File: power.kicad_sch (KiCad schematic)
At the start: 58 parts

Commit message: Schematic is basically feature complete
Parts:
- removed C? (x2): 10u, Capacitor_SMD:C_0402_1005Metric, symbol Device:C
- removed R? (x2): 0R1, Resistor_SMD:R_0402_1005Metric, symbol Device:R
- added L10, L5, L6, L7, L8, L9: 220, Inductor_SMD:L_0603_1608Metric, symbol Device:L_Ferrite
- C101, C71, C81, C91: renamed from C?; value 0u1 -> 10u; JLCPCB (none) -> C15525
- R73, R83, R93, R94: renamed from R?; footprint Resistor_SMD:R_0402_1005Metric -> Resistor_SMD:R_0603_1608Metric
- TP10, TP7, TP8, TP9: renamed from TP?; now left out of the parts list
- TP? (x2): now left out of the parts list
- U7, U9: renamed from U?; value TPS7A91 -> TPS7A8801RTJR; footprint Package_DFN_QFN:Texas_S-PDSO-N10_EP1.2x2mm -> RTJ0020D; symbol Parts:TPS7A91 -> Parts:TPS7A8801RTJR
- gave numbers to parts that had none: 36
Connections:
- net +3V3: now also U7.14 (OUT1), U7.15 (OUT1); no longer U7.1 (OUT), U7.2 (OUT)
- net CGEN_1V8: now also U9.11 (OUT2), U9.12 (OUT2); no longer U9.1 (OUT), U9.2 (OUT)
- net CGEN_3V3: now also U9.14 (OUT1), U9.15 (OUT1); no longer U9.1 (OUT), U9.2 (OUT)
- net GND: now also U7.13 (GND), U7.21 (GND), U7.21 (GND), U7.3 (GND), U9.13 (GND), U9.21 (GND), U9.21 (GND), U9.3 (GND); no longer U7.11 (GND), U7.11 (GND), U7.4 (GND), U7.4 (GND), U9.11 (GND), U9.11 (GND), U9.4 (GND), U9.4 (GND)
- net VBUS: now also L5.1, L6.1
- net ≈2.1V: now also L10.1; no longer C101.1, U9.10 (IN), U9.6 (SS_CTRL), U9.7 (EN), U9.9 (IN)
- net ≈3.6V: now also L7.1, L8.1, L9.1; no longer C71.1, C81.1, C91.1, U7.10 (IN), U7.10 (IN), U7.6 (SS_CTRL), U7.6 (SS_CTRL), U7.7 (EN), U7.7 (EN), U7.9 (IN), U7.9 (IN), U9.10 (IN), U9.6 (SS_CTRL), U9.7 (EN), U9.9 (IN)
- net at C72.2, R71.2, R72.1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: now also U7.16 (FB1); no longer U7.3 (FB)
- net at C94.1: now also U9.19 (NR_SS1); no longer U9.8 (NR/SS)
- net at C61.1, U6.1 (EN), U6.3 (VIN)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: now also L6.2
- net at C82.2, R81.2, R82.1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: now also U7.10 (FB2); no longer U7.3 (FB)
- net IN2: now reaches U7.5 (IN2)
- net IN2: now also C101.1, C81.1, U7.4 (IN2), U7.6 (EN2), U7.7 (NR_SS2), U9.4 (IN2), U9.5 (IN2), U9.6 (EN2), U9.7 (NR_SS2), L10.2, L8.2
- net at C92.2, R91.2, R92.1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: now also U9.16 (FB1); no longer U9.3 (FB)
- net at C102.2, R101.2, R102.1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: now also U9.10 (FB2); no longer U9.3 (FB)
- net at C74.1: now also U7.19 (NR_SS1); no longer U7.8 (NR/SS)
- net at C51.1, U5.1 (EN), U5.3 (VIN)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: now also L5.2
- net TXCO_3V3 renamed TCXO_3V3
- net TCXO_3V3: now also U7.11 (OUT2), U7.12 (OUT2); no longer U7.1 (OUT), U7.2 (OUT)
- new net IN1: C71.1, C91.1, L7.2, L9.2, U7.1 (IN1), U7.18 (SS_CTRL1), U7.2 (IN1), U7.20 (EN1), U9.1 (IN1), U9.18 (SS_CTRL1), U9.2 (IN1), U9.20 (EN1)
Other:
- moved on the sheet: C101, C102, C103, C104, C61, C62, C63, C64, C65, C91, C92, C93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

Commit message: Sorting out the part placement....
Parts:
- removed C52, C62: 100p, Capacitor_SMD:C_0402_1005Metric, symbol Device:C
- removed C54, C55, C64, C65: 10u, Capacitor_SMD:C_0402_1005Metric, symbol Device:C
- removed L8, L9: 220, Inductor_SMD:L_0603_1608Metric, symbol Device:L_Ferrite
- added C75: 1u, Capacitor_SMD:C_0402_1005Metric, symbol Device:C
- C53: value 10u -> 47u; footprint Capacitor_SMD:C_0402_1005Metric -> Capacitor_SMD:C_0805_2012Metric; JLCPCB C15525 -> (none)
- C63: value 10u -> 47u; footprint Capacitor_SMD:C_0402_1005Metric -> Capacitor_SMD:C_0805_2012Metric; JLCPCB C15525 -> C16780
- C81, C91: value 10u -> 1u; JLCPCB C15525 -> (none)
- L10, L5, L6, L7: symbol Device:L_Ferrite -> Parts:L_Ferrite_Power
- R61: value ? -> 82k
- R62: value 51k -> 50k
- R73, R83, R93: value 10k -> ???
- TP10, TP7, TP8, TP9: footprint (none) -> Parts:TestPoint
- TP5, TP6: renamed from TP?; footprint (none) -> Parts:TestPoint
- U7, U9: footprint RTJ0020D -> Package_DFN_QFN:QFN-20-1EP_4x4mm_P0.5mm_EP2.7x2.7mm; JLCPCB C2878140 -> (none)
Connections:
- net GND: now also U5.5 (GND), U5.6 (GND), U5.9 (PAD), U6.5 (GND), U6.6 (GND), U6.9 (PAD), U7.18 (SS_CTRL1), U7.8 (SS_CTRL2), U9.18 (SS_CTRL1), U9.8 (SS_CTRL2), C75.2
- net Fb3V3: now reaches C72.2, R71.2, R72.1, R73.1, U7.16 (FB1)
- net FbTC3: now reaches C82.2, R81.2, R82.1, R83.1, U7.10 (FB2)
- net at C84.1: now also U7.7 (NR_SS2); no longer U7.8 (SS_CTRL2)
- net FbCG3: now reaches C92.2, R91.2, R92.1, R93.1, U9.16 (FB1)
- net In2V1: now reaches C61.1, L6.2, U6.1 (EN), U6.3 (VIN), U6.4 (VIN)
- net Fb21: now reaches R61.2, R62.1, U6.7 (FB)
- net FbCG18: now reaches C102.2, R101.2, R102.1, R94.1, U9.10 (FB2)
- net at C104.1: now also U9.7 (NR_SS2); no longer U9.8 (SS_CTRL2)
- net Fb36: now reaches R51.2, R52.1, U5.7 (FB)
- net In3V6: now reaches C51.1, L5.2, U5.1 (EN), U5.3 (VIN), U5.4 (VIN)
- net IN1 renamed In3V3
- net In3V3: now also C81.1, U7.4 (IN2), U7.5 (IN2), U7.6 (EN2), C75.1; no longer U7.18 (SS_CTRL1), U9.18 (SS_CTRL1)
- removed net IN2: C101.1, C81.1, L10.2, U7.4 (IN2), U7.5 (IN2), U7.6 (EN2), U7.7 (NR_SS2), U9.4 (IN2), U9.5 (IN2), U9.6 (EN2), U9.7 (NR_SS2)
- net VBUS renamed VBus
- net ≈2.1V renamed 2V1
- net ≈3.6V renamed 3V6
- new net In1V8: C101.1, L10.2, U9.4 (IN2), U9.5 (IN2), U9.6 (EN2)
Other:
- note added: "TODO - datasheet says no FF caps."
- moved on the sheet: C53, C63, C71, L10, L7, R51, R52, R61, R62, TP5, TP6

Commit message: Placement looks sane.
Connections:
- net +3V3: now also U7.11 (OUT2), U7.12 (OUT2); no longer U7.14 (OUT1), U7.15 (OUT1)
- net CGEN_1V8: now also U7.14 (OUT1), U7.15 (OUT1); no longer U9.11 (OUT2), U9.12 (OUT2)
- net CGEN_3V3: now also U9.11 (OUT2), U9.12 (OUT2); no longer U9.14 (OUT1), U9.15 (OUT1)
- net Fb3V3: now also U7.10 (FB2); no longer U7.16 (FB1)
- net FbCG18: now also U7.16 (FB1); no longer U9.10 (FB2)
- net FbCG3: now also U9.10 (FB2); no longer U9.16 (FB1)
- net FbTC3: now also U9.16 (FB1); no longer U7.10 (FB2)
- net In1V8: now also U7.1 (IN1), U7.2 (IN1), U7.20 (EN1); no longer U9.4 (IN2), U9.5 (IN2), U9.6 (EN2)
- net In3V3: now also U9.4 (IN2), U9.5 (IN2), U9.6 (EN2); no longer U7.1 (IN1), U7.2 (IN1), U7.20 (EN1)
- net TCXO_3V3: now also U9.14 (OUT1), U9.15 (OUT1); no longer U7.11 (OUT2), U7.12 (OUT2)
- net at C94.1: now also U9.7 (NR_SS2); no longer U9.19 (NR_SS1)
- net at U7.19 (NR_SS1): now also C104.1; no longer C74.1
- net at C84.1: now also U9.19 (NR_SS1); no longer U7.7 (NR_SS2)
- new net: C74.1, U7.7 (NR_SS2)
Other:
- moved on the sheet: U7A, U7B, U9A, U9B

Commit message: Down to the dregs and clean-ups.
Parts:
- C53: JLCPCB (none) -> C16780
- C72, C82, C92: JLCPCB (none) -> C15195
- C74, C84, C94: JLCPCB (none) -> C307331
- C75, C81, C91: JLCPCB (none) -> C52923
- C80: renamed from C104; JLCPCB (none) -> C307331
- C85: renamed from C102; JLCPCB (none) -> C15195
- R51: value 180k -> 120k; JLCPCB (none) -> C25750
- R52: value 51k -> 33k; JLCPCB (none) -> C25779
- R61: value 82k -> 56k; JLCPCB (none) -> C25796
- R62: value 50k -> 33k; JLCPCB (none) -> C25779
- R71, R81, R91: value 3k6 -> 15k; JLCPCB (none) -> C25756
- R72, R82, R92: value 1k2 -> 5k1; JLCPCB (none) -> C25905
- R73, R83, R93: value ??? -> 82k; JLCPCB (none) -> C23254; now fitted; now in the parts list
- R85: renamed from R102; value 1k5 -> 7k5; JLCPCB (none) -> C25918
- R86: renamed from R101; value 1k8 -> 8k2; JLCPCB (none) -> C25924
- R87: renamed from R94; value 10k -> 51k; JLCPCB (none) -> C23196; now fitted; now in the parts list
- U5, U6: JLCPCB (none) -> C468248
- U7, U9: JLCPCB (none) -> C485919
- renumbered C101 to C79, C103 to C86

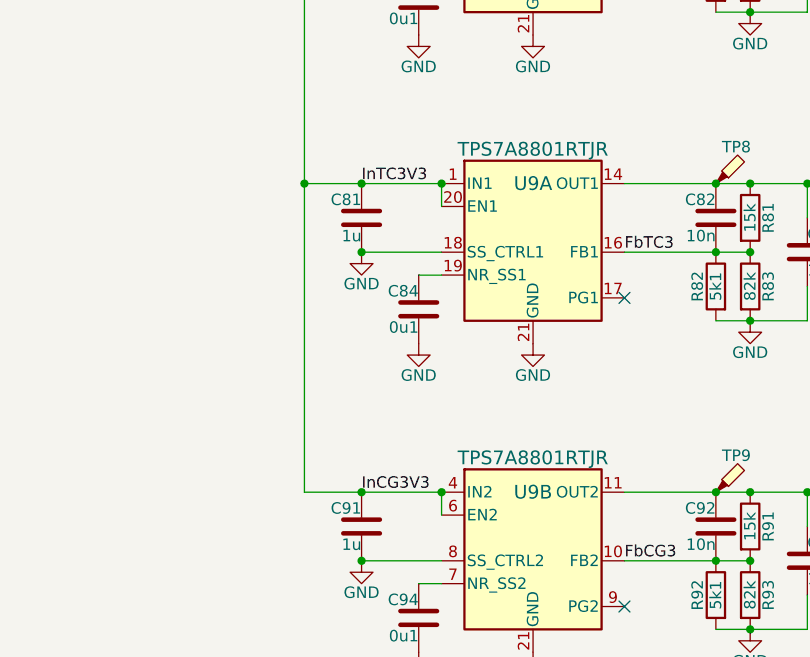
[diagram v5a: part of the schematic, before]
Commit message: Add a U.Fl connector for fun.
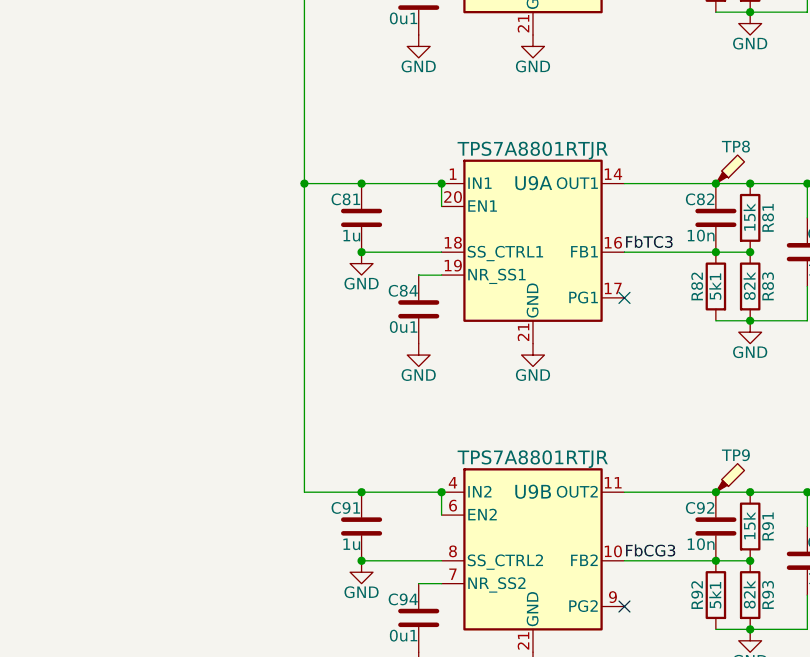
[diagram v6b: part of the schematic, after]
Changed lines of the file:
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@@
-		)
-	)
-	(label "InTC3V3"
-		(at 123.19 59.69 0)
-		(effects
-			(font
-				(size 1.27 1.27)
-			)
-			(justify left bottom)
 		)
 	)
@@
 		(effects
 			(font
-				(size 1.27 1.27)
-			)
-			(justify left bottom)
-		)
-	)
-	(label "InCG3V3"
-		(at 123.19 93.98 0)
-		(effects
-			(font

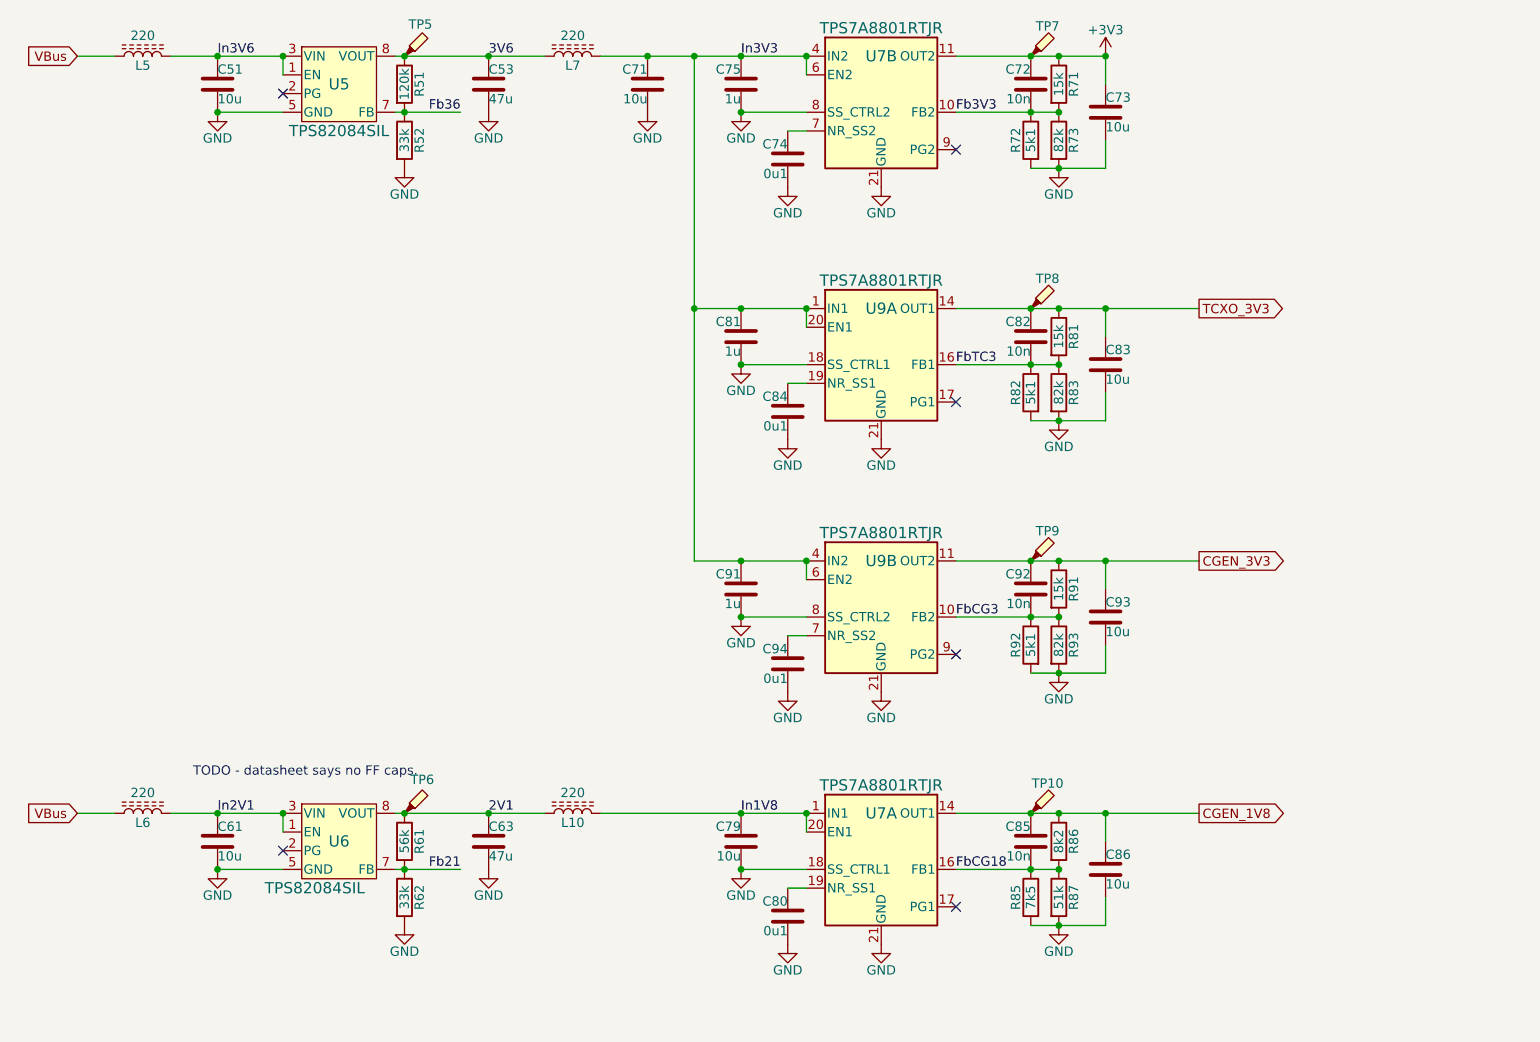
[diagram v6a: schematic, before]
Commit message: DRC clean-up.  Only silk-screen noise left.
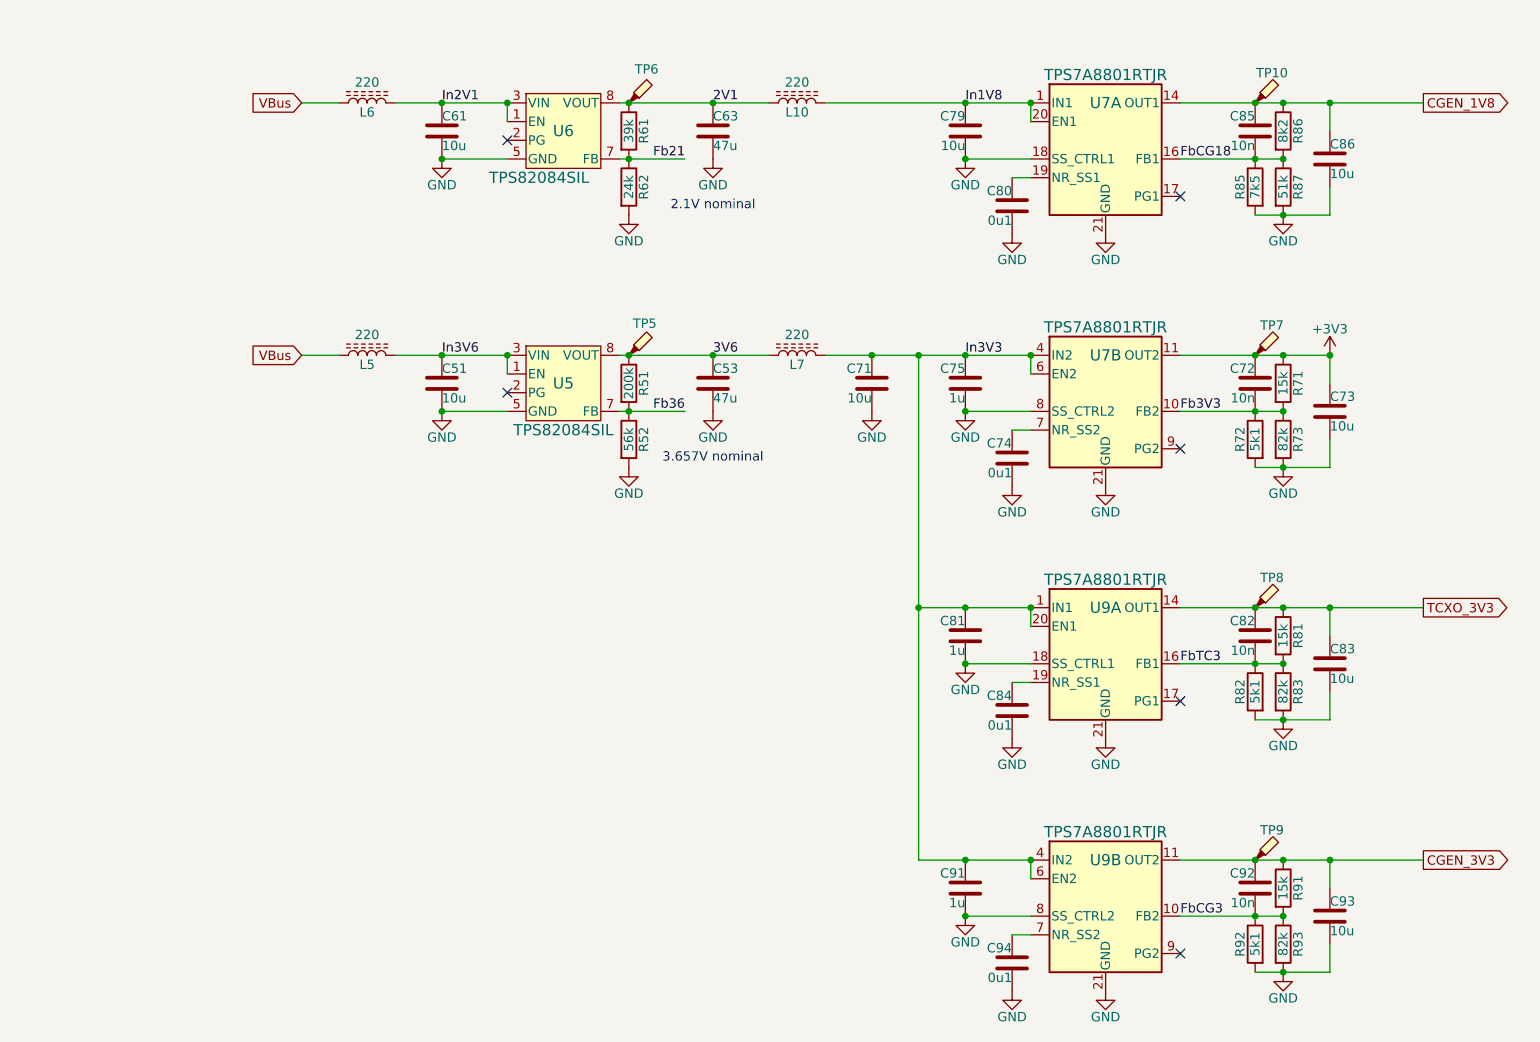
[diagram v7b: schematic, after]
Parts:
- R51: value 120k -> 200k; JLCPCB C25750 -> (none)
- R52: value 33k -> 56k; JLCPCB C25779 -> (none)
- R61: value 56k -> 39k
- R62: value 33k -> 24k; JLCPCB C25779 -> (none)
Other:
- note added: "2.1V nominal"
- note added: "3.657V nominal"
- note removed: "TODO - datasheet says no FF caps."
- moved on the sheet: C51, C53, C61, C63, C71, C72, C73, C74, C75, C79, C80, C81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

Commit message: Squeeze in a connector to break out GPS.
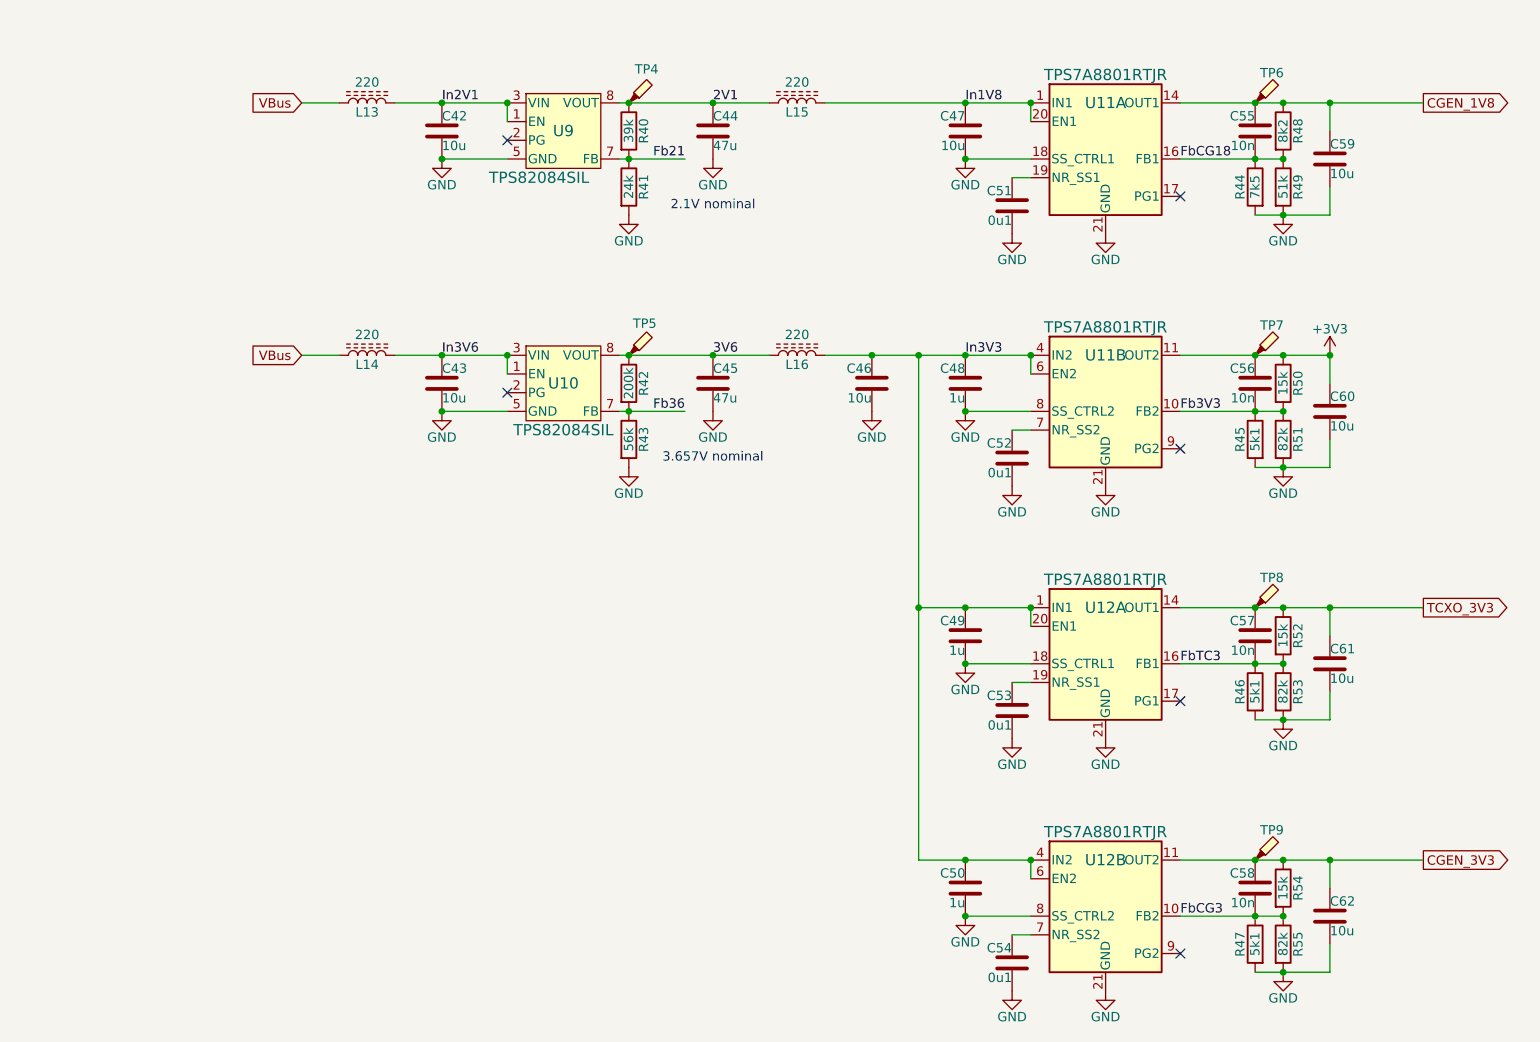
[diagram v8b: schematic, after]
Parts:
- renumbered C61 to C42, C51 to C43, C63 to C44, C53 to C45, C71 to C46, C79 to C47, C75 to C48, C81 to C49, C91 to C50, C80 to C51, C74 to C52, C84 to C53, C94 to C54, C85 to C55, C72 to C56, C82 to C57, C92 to C58, C86 to C59, C73 to C60, C83 to C61, C93 to C62, L6 to L13, L5 to L14, L10 to L15, L7 to L16, R61 to R40, R62 to R41, R51 to R42, R52 to R43, R85 to R44, R72 to R45, R82 to R46, R92 to R47, R86 to R48, R87 to R49, R71 to R50, R73 to R51, R81 to R52, R83 to R53, R91 to R54, R93 to R55, TP6 to TP4, TP10 to TP6, U5 to U10, U7 to U11, U9 to U12, U6 to U9
